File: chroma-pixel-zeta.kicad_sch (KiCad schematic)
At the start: 4 parts

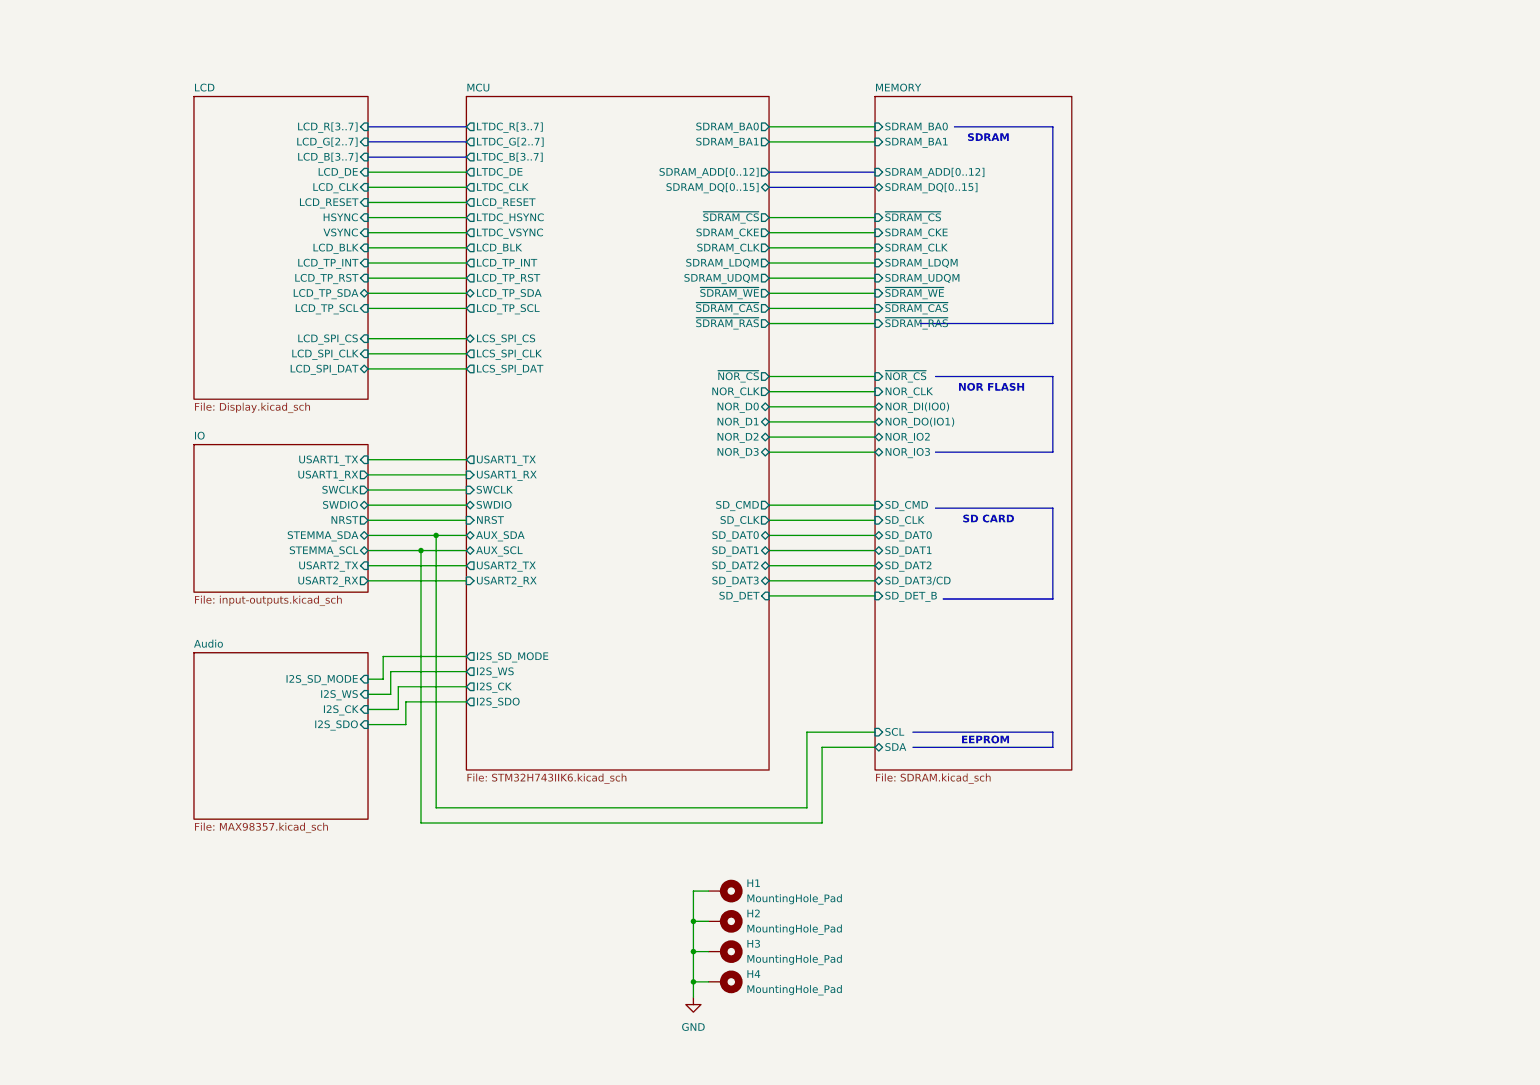
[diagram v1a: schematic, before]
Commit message: Cleaning schematic, added more independently schematics
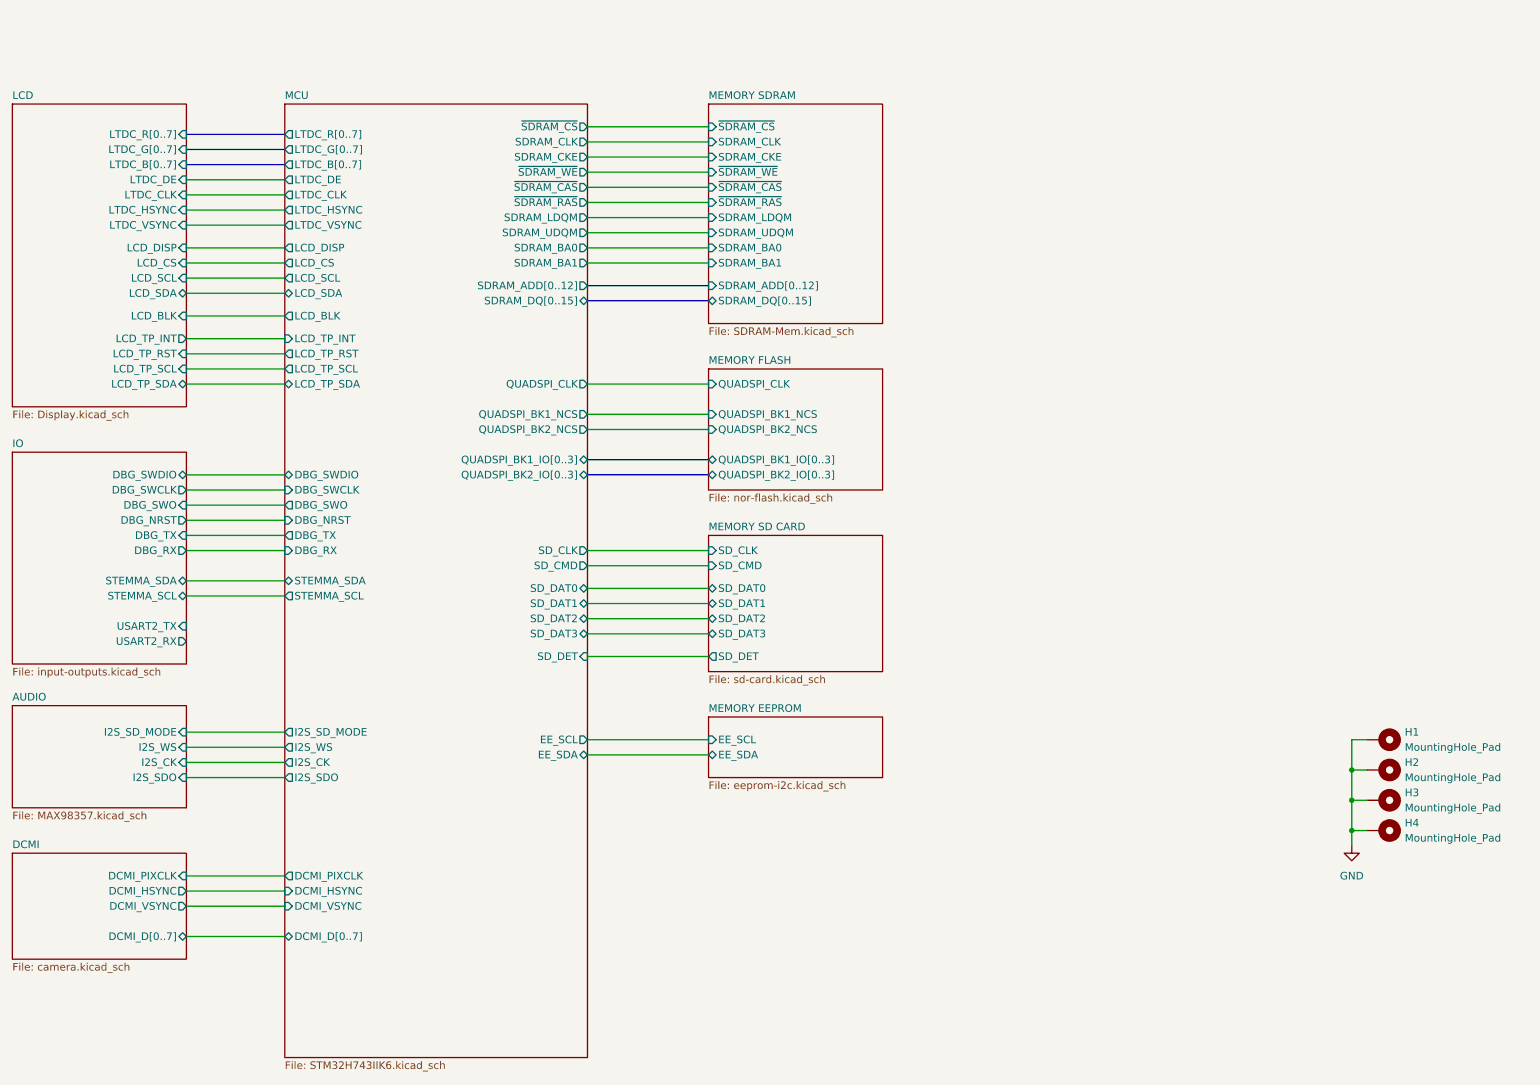
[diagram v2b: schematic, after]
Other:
- sheet Audio renamed AUDIO
- removed sheet MEMORY
- added sheet DCMI (camera.kicad_sch)
- added sheet MEMORY EEPROM (eeprom-i2c.kicad_sch)
- added sheet MEMORY FLASH (nor-flash.kicad_sch)
- added sheet MEMORY SD CARD (sd-card.kicad_sch)
- added sheet MEMORY SDRAM (SDRAM-Mem.kicad_sch)
- sheet IO ports: added DBG_NRST, DBG_RX, DBG_SWCLK, DBG_SWDIO, DBG_SWO, DBG_TX; removed NRST, SWCLK, SWDIO, USART1_RX, USART1_TX
- sheet LCD ports: added LCD_CS, LCD_DISP, LCD_SCL, LCD_SDA, LTDC_B[0..7], LTDC_CLK, LTDC_DE, LTDC_G[0..7], LTDC_HSYNC, LTDC_R[0..7], LTDC_VSYNC; removed HSYNC, LCD_B[3..7], LCD_CLK, LCD_DE, LCD_G[2..7], LCD_RESET, LCD_R[3..7], LCD_SPI_CLK, LCD_SPI_CS, LCD_SPI_DAT, VSYNC
- sheet MCU ports: added DBG_NRST, DBG_RX, DBG_SWCLK, DBG_SWDIO, DBG_SWO, DBG_TX, DCMI_D[0..7], DCMI_HSYNC, DCMI_PIXCLK, DCMI_VSYNC, EE_SCL, EE_SDA, LCD_CS, LCD_DISP, LCD_SCL, LCD_SDA, LTDC_B[0..7], LTDC_G[0..7], LTDC_R[0..7], QUADSPI_BK1_IO[0..3], QUADSPI_BK1_NCS, QUADSPI_BK2_IO[0..3], QUADSPI_BK2_NCS, QUADSPI_CLK, STEMMA_SCL, STEMMA_SDA; removed AUX_SCL, AUX_SDA, LCD_RESET, LCS_SPI_CLK, LCS_SPI_CS, LCS_SPI_DAT, LTDC_B[3..7], LTDC_G[2..7], LTDC_R[3..7], NOR_CLK, NOR_D0, NOR_D1, NOR_D2, NOR_D3, NRST, SWCLK, SWDIO, USART1_RX, USART1_TX, USART2_RX, USART2_TX, ~{NOR_CS}
- note removed: "EEPROM"
- note removed: "NOR FLASH"
- note removed: "SD CARD"
- note removed: "SDRAM"
- moved on the sheet: H1, H2, H3, H4

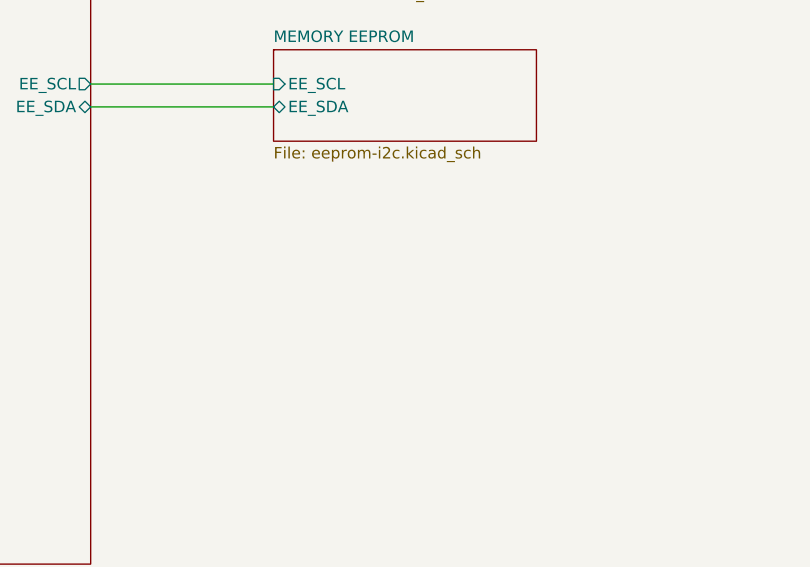
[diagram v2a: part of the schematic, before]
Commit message: Layout SDRAM
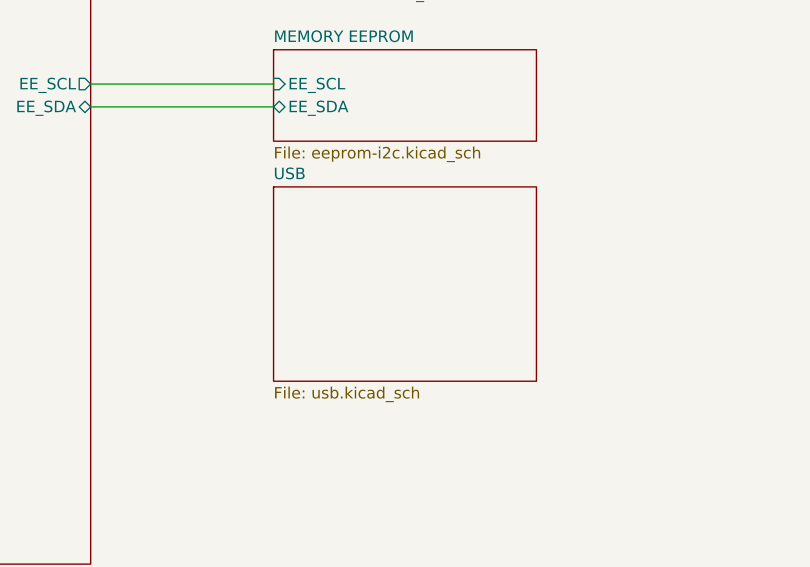
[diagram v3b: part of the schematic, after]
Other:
- added sheet USB (usb.kicad_sch)
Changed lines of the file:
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@@
+	)
+	(sheet
+		(at 144.78 146.05)
+		(size 29.21 21.59)
+		(fields_autoplaced yes)
+		(stroke
+			(width 0.1524)
+			(type solid)
+		)
+		(fill
+			(color 0 0 0 0.0000)
+		)
+		(property "Sheetname" "USB"
+			(at 144.78 145.3384 0)
+			(effects
+				(font
+					(size 1.27 1.27)
+				)
+				(justify left bottom)
+			)
+		)
+		(property "Sheetfile" "usb.kicad_sch"
+			(at 144.78 168.2246 0)
+			(effects
+				(font
+					(size 1.27 1.27)
+				)
+				(justify left top)
+			)
+		)
+		(instances
+			(project "chroma-pixel-zeta"
+				(path "/70094798-b7e4-48a4-a512-b8f48be18f9f"
+					(page "11")
+				)
+			)
+		)
 	)
 	(sheet

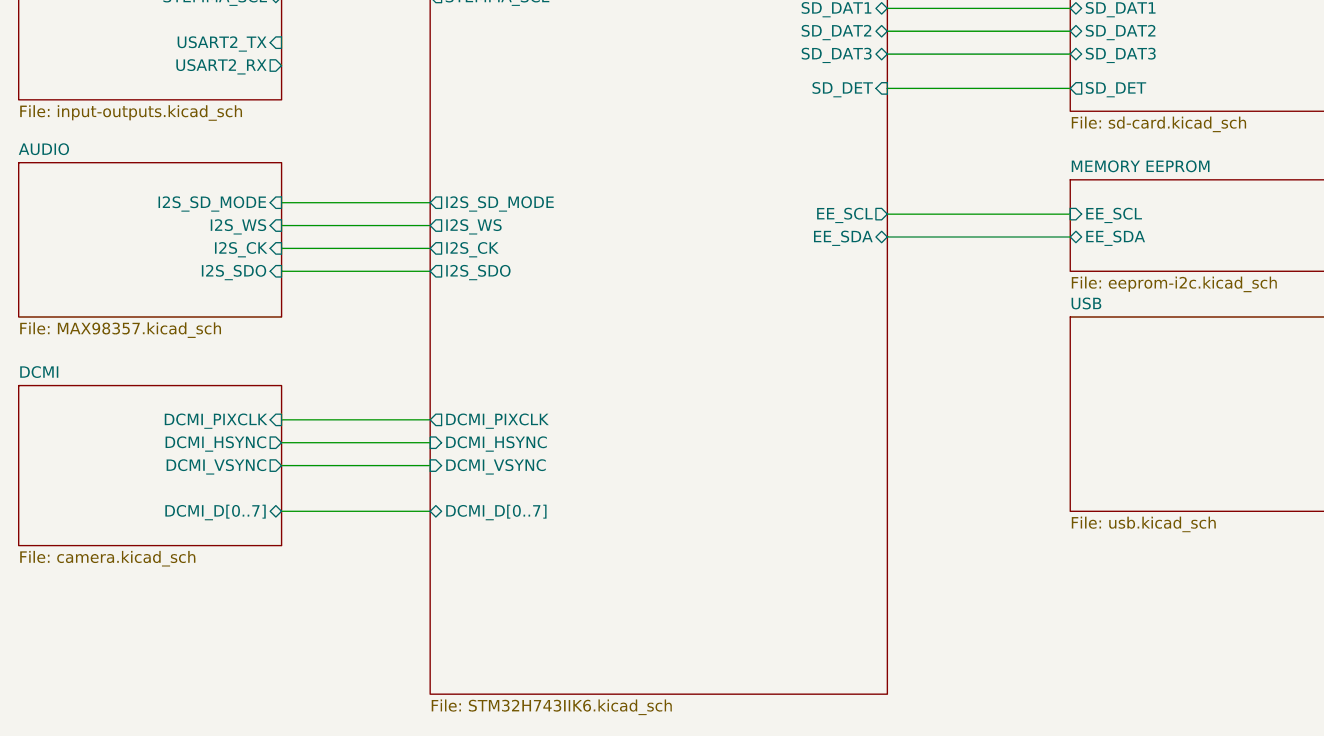
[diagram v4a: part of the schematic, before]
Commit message: Changes: USB C to midmount, CR1220 socket, flip MCU to shorten the LCD traces
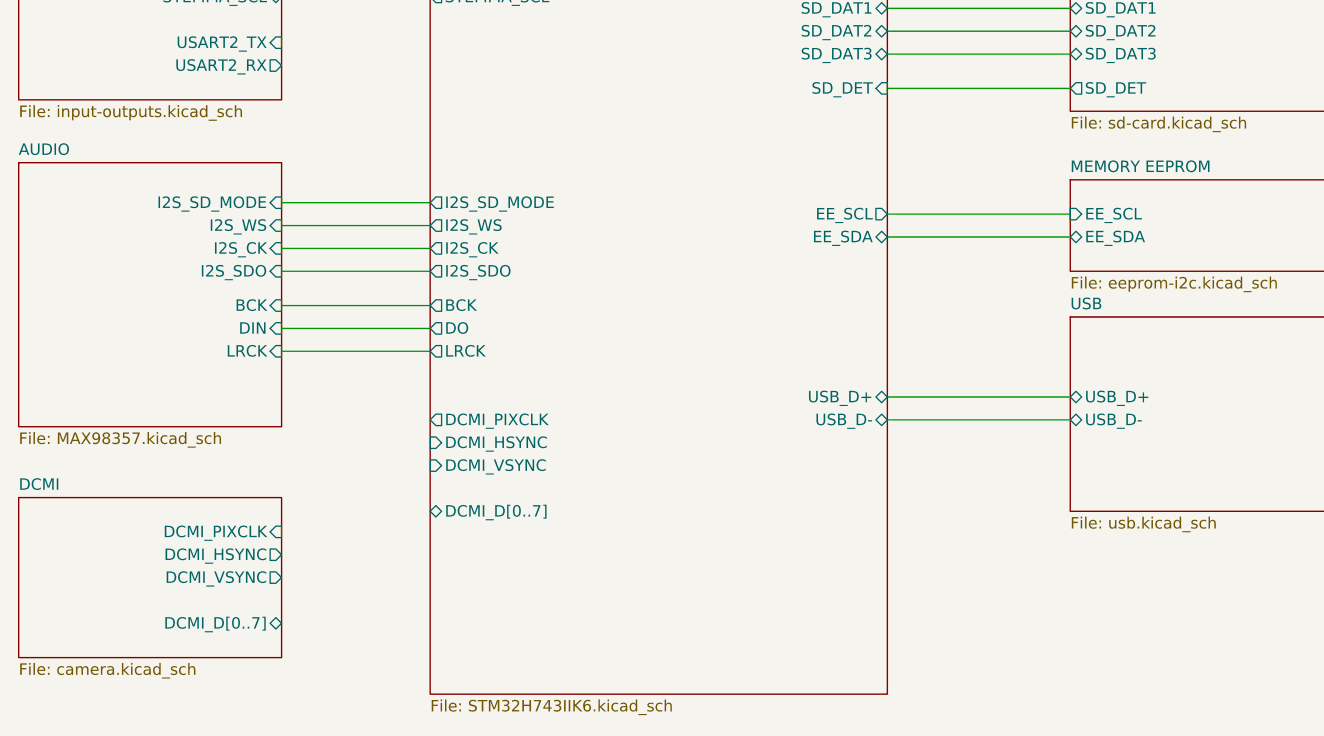
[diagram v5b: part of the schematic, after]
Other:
- sheet AUDIO ports: added BCK, DIN, LRCK; removed none
- sheet MCU ports: added BCK, DO, LRCK, USB_D+, USB_D-; removed none
- sheet USB ports: added USB_D+, USB_D-; removed none

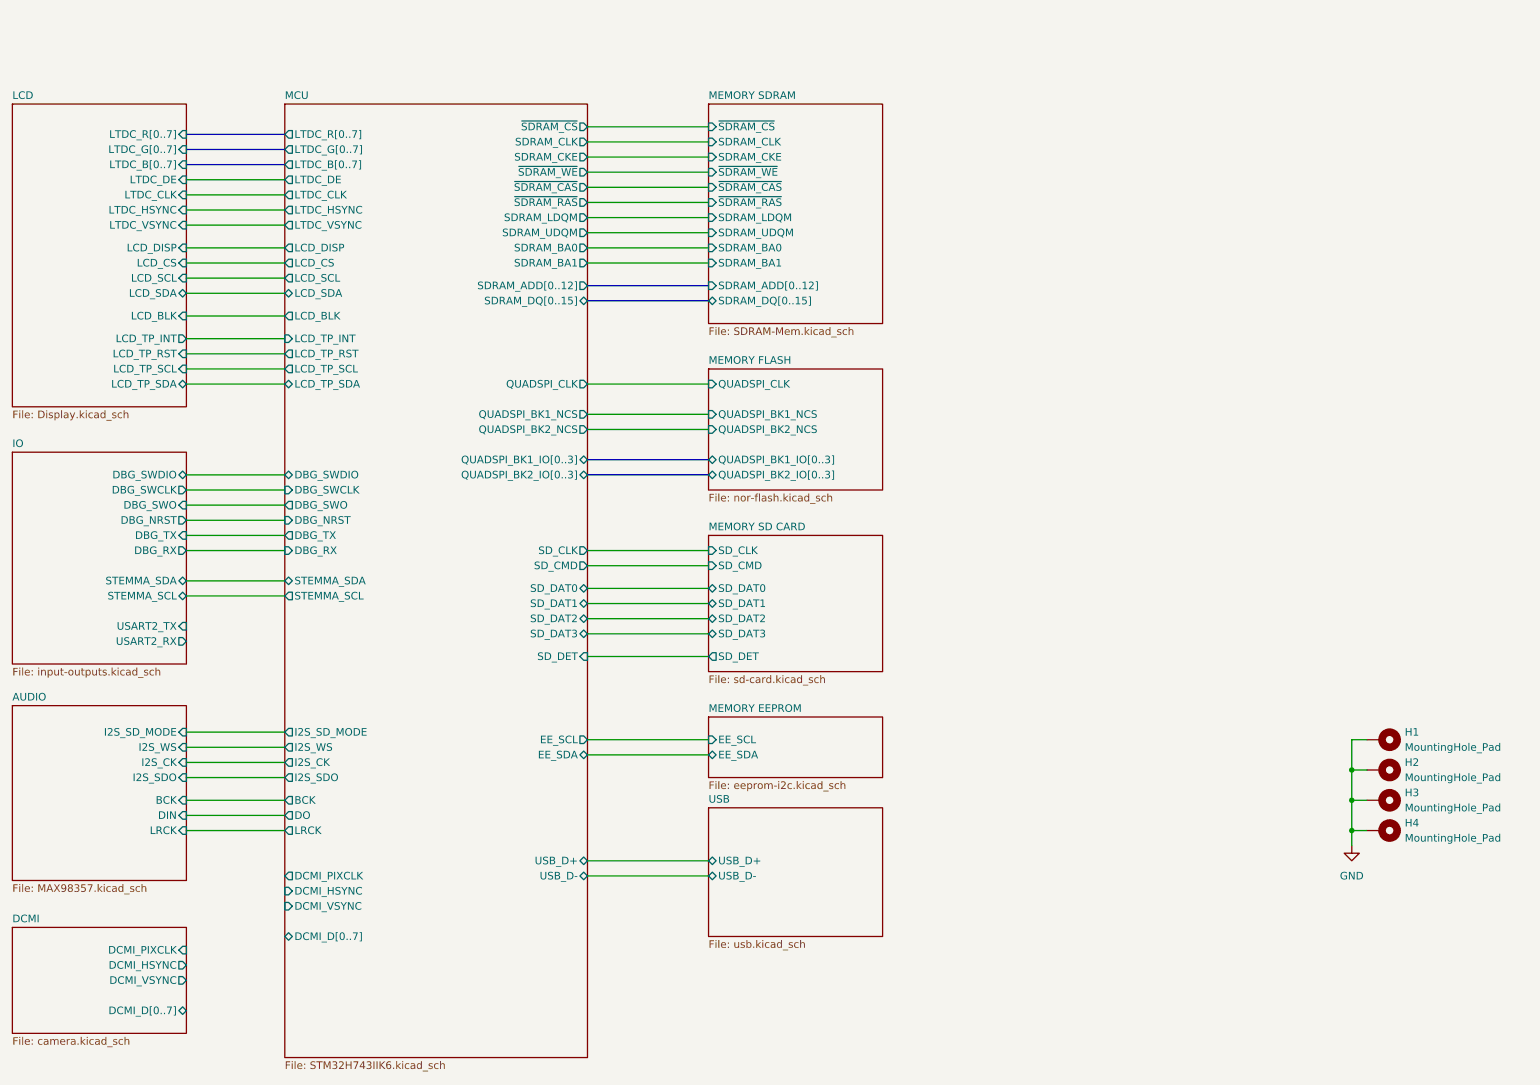
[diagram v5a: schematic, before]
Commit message: Button, LED, i2s audio, LCD & SD ctrl left
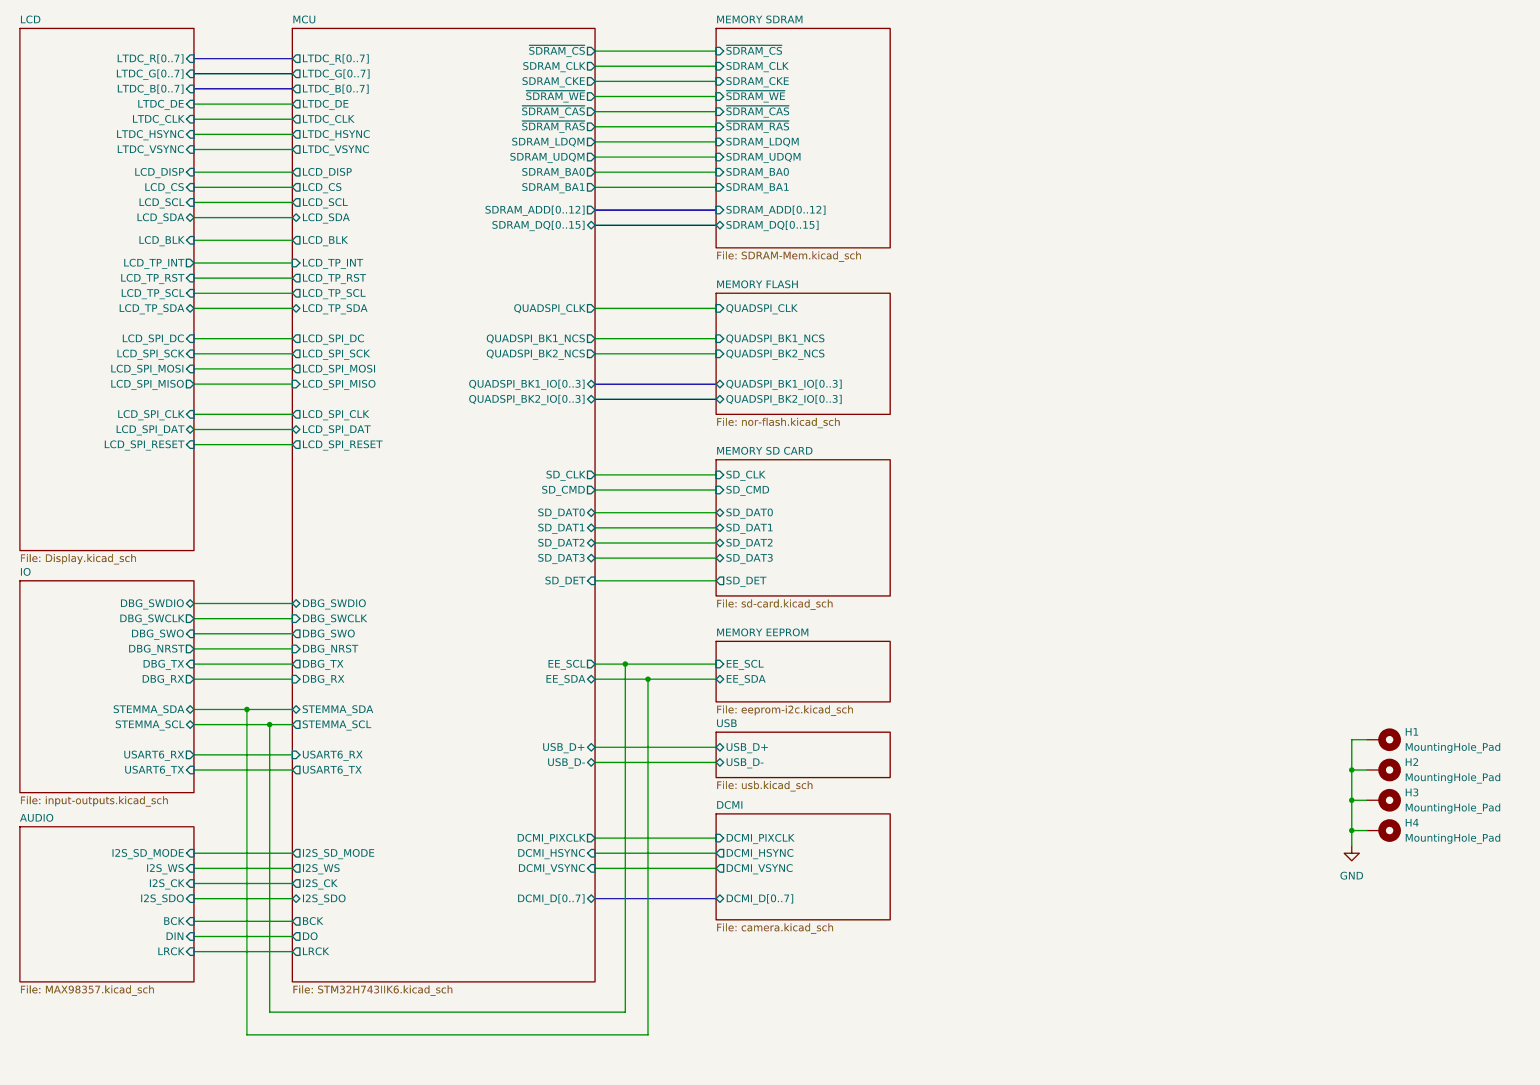
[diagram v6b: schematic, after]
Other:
- sheet IO ports: added USART6_RX, USART6_TX; removed USART2_RX, USART2_TX
- sheet LCD ports: added LCD_SPI_CLK, LCD_SPI_DAT, LCD_SPI_DC, LCD_SPI_MISO, LCD_SPI_MOSI, LCD_SPI_RESET, LCD_SPI_SCK; removed none
- sheet MCU ports: added LCD_SPI_CLK, LCD_SPI_DAT, LCD_SPI_DC, LCD_SPI_MISO, LCD_SPI_MOSI, LCD_SPI_RESET, LCD_SPI_SCK, USART6_RX, USART6_TX; removed none
